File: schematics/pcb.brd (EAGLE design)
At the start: 69.8 x 100 mm, 39 parts, among them IC1 7805TV, IC2 4050D, IC3 LP298XS, Q1 16Mhz, Q2 16Mhz, X1 MICROSD

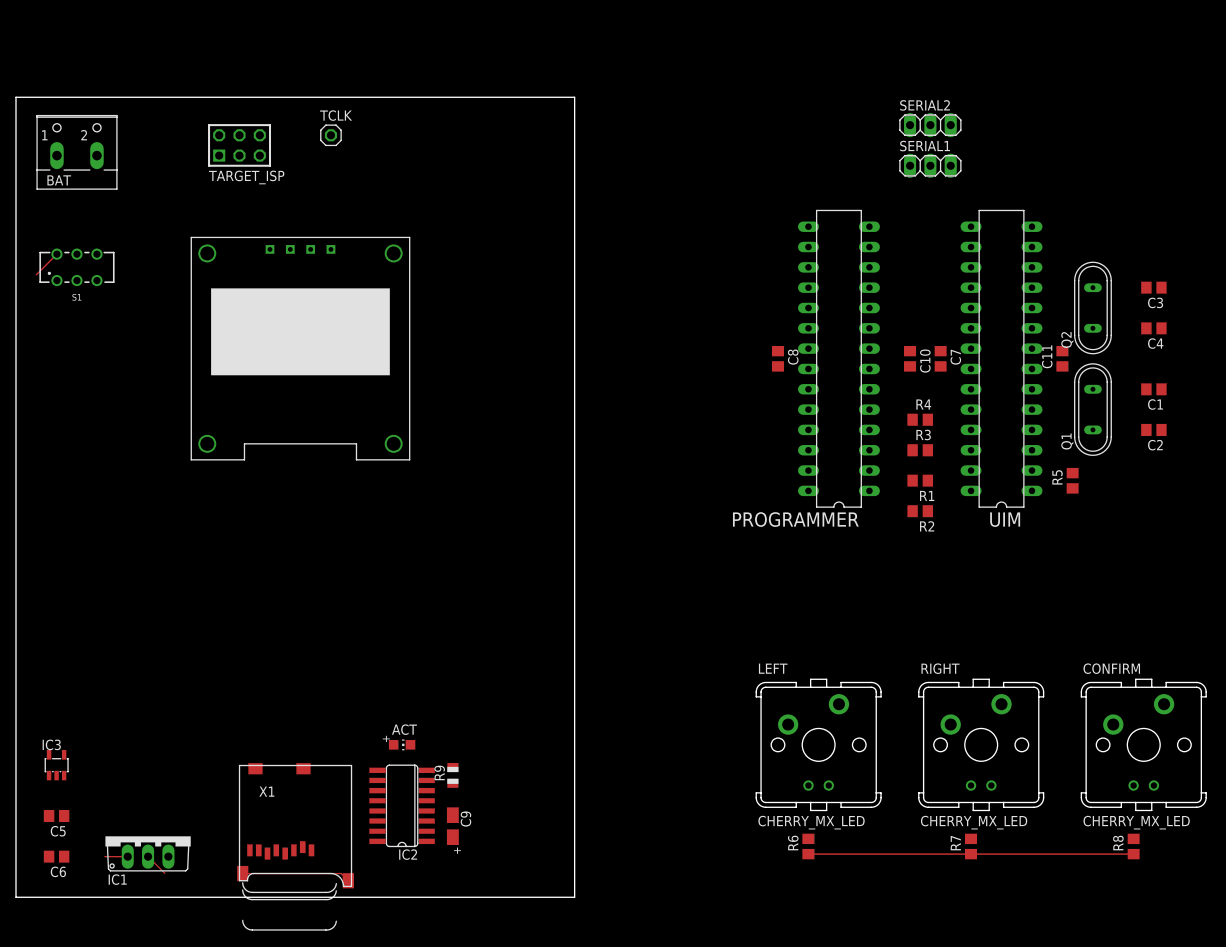
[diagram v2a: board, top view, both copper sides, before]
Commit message: PCB part placements and partial routing
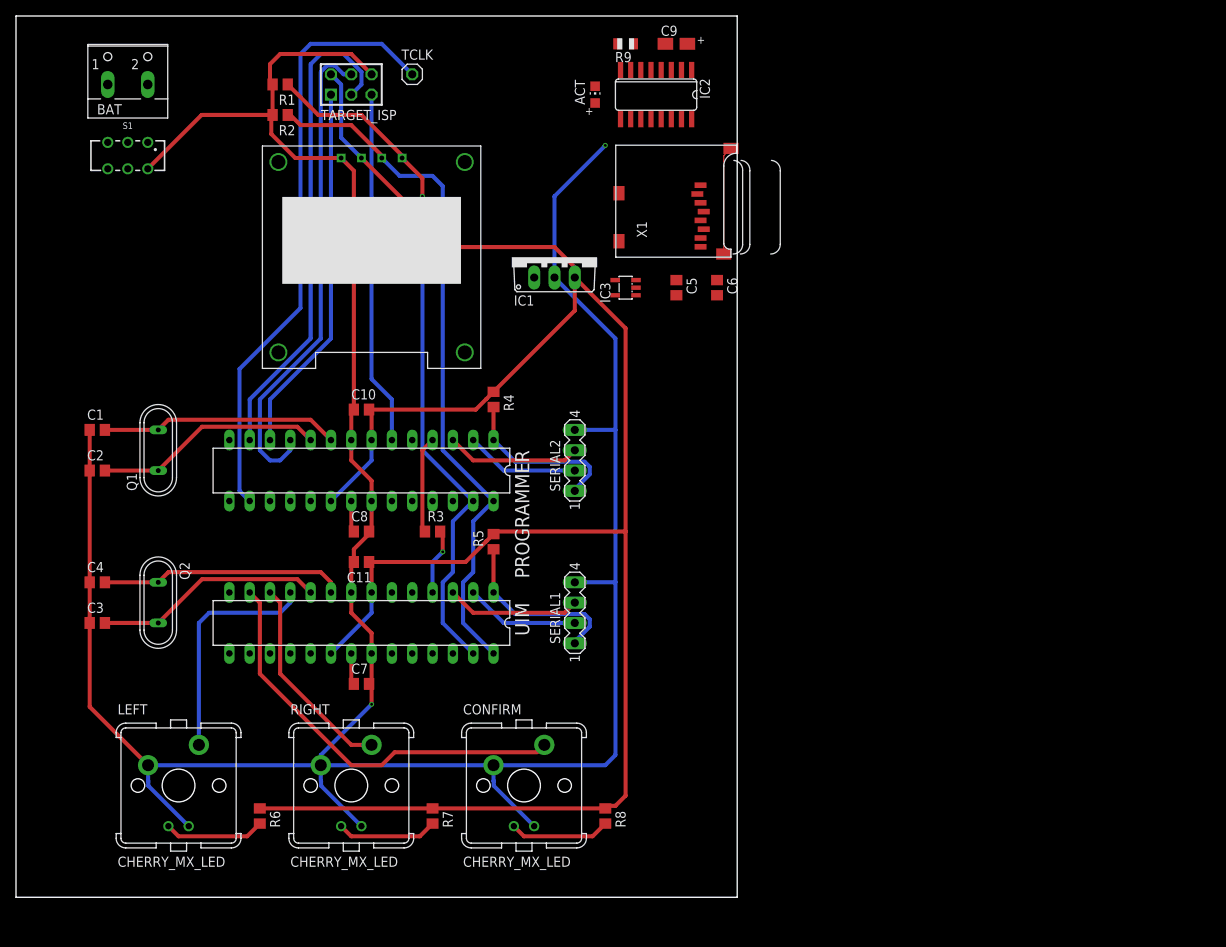
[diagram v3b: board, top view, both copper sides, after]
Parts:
- SERIAL1, SERIAL2: device pinhead:1X03 -> con-lstb:MA04-1
- moved C3 138.6 mm to (10.2, 34.3), turned to 0 degrees
- moved C4 135.8 mm to (10.2, 39.4), turned to 0 degrees
- moved C1 132.2 mm to (10.2, 58.4), turned to 0 degrees
- moved C2 132.2 mm to (10.2, 53.3), turned to 0 degrees
- moved Q2 122.5 mm to (17.8, 36.8), turned to 270 degrees
- moved Q1 117.0 mm to (17.8, 55.9)
- moved C6 109.0 mm to (87.6, 76.2), turned to 270 degrees
- moved C5 101.8 mm to (82.5, 76.2), turned to 270 degrees
- moved C9 101.7 mm to (82.5, 106.7), turned to 0 degrees
- moved IC2 94.4 mm to (80.0, 100.3), turned to 180 degrees
- moved R2 94.1 mm to (33.0, 97.8)
- moved R1 94.1 mm to (33.0, 101.6)
- moved R9 94.0 mm to (76.2, 106.7), turned to 180 degrees
- moved IC3 92.8 mm to (76.2, 76.2), turned to 90 degrees
- moved C11 91.2 mm to (43.2, 41.9), turned to 180 degrees
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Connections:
- removed net N$17: BAT.1, S1.5
- removed net PWRIN: C5.1, IC1.1, S1.4
- new net 9V+: C5.1, IC1.1, S1.1
- new net BAT+: BAT.1, S1.2
- new net BAT-: BAT.2, S1.5
- net GND: now also S1.4, SERIAL1.4, SERIAL2.4; no longer BAT.2
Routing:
- net GND: track 16.6 -> 373.3 mm, vias 0 -> 2
- net +5V: track 40.6 -> 256.6 mm
- net N$1: track 0.00 -> 87.4 mm
- net N$2: track 0.00 -> 87.0 mm, vias 0 -> 1
- net N$28: track 0.00 -> 75.6 mm
- net N$13: track 0.00 -> 61.3 mm
- net B$1: track 0.00 -> 61.2 mm
- net N$16: track 0.00 -> 52.0 mm
- net N$12: track 0.00 -> 46.3 mm
- net N$14: track 0.00 -> 44.2 mm
- net N$11: track 0.00 -> 30.6 mm
- net N$7: track 0.00 -> 29.8 mm
- net N$9: track 0.00 -> 29.0 mm
- net N$10: track 0.00 -> 28.7 mm
- net N$8: track 0.00 -> 28.7 mm
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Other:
- board size 69.8 x 100 mm -> 90.2 x 110.2 mm

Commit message: Finished PCB routing
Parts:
- moved C6 25.2 mm to (63.5, 69.1), turned to 180 degrees
- moved C5 22.1 mm to (61.0, 71.6), turned to 0 degrees
- moved C9 17.5 mm to (66.0, 100.8), turned to 270 degrees
- moved R9 10.9 mm to (81.3, 97.0), turned to 90 degrees
- moved ACT 9.07 mm to (81.3, 102.1), turned to 180 degrees
- moved IC2 6.37 mm to (73.7, 100.8), turned to 0 degrees
- moved X1 5.47 mm to (69.8, 78.0)
- moved IC1 5.47 mm to (62.2, 78.0)
- moved U$1 5.47 mm to (39.4, 78.0)
- moved R2 5.47 mm to (27.9, 95.8)
- moved BAT 5.47 mm to (8.89, 100.8)
- moved Q1 5.47 mm to (12.7, 53.8)
- moved TCLK 5.47 mm to (44.5, 100.8)
- moved R6 5.47 mm to (25.4, 8.13)
- moved C1 5.47 mm to (5.08, 56.4)
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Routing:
- net DO: track 0.00 -> 175.6 mm, vias 0 -> 1
- net CLK: track 0.00 -> 145.0 mm, vias 0 -> 2
- net DI: track 0.00 -> 129.5 mm, vias 0 -> 1
- net GND: track 373.3 -> 450.5 mm, vias 2 -> 4
- net 9V+: track 0.00 -> 64.5 mm
- net +3V3: track 0.00 -> 43.8 mm, vias 0 -> 2
- net BAT-: track 0.00 -> 28.4 mm
- net N$24: track 0.00 -> 20.8 mm
- net +5V: track 256.6 -> 276.4 mm
- net N$25: track 0.00 -> 19.4 mm
- net N$27: track 0.00 -> 16.6 mm
- net BAT+: track 0.00 -> 8.28 mm
- net N$23: track 0.00 -> 8.10 mm
- net N$26: track 0.00 -> 3.03 mm
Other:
- board size 90.2 x 110.2 mm -> 86.3 x 110.2 mm
